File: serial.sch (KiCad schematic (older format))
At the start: 1 part

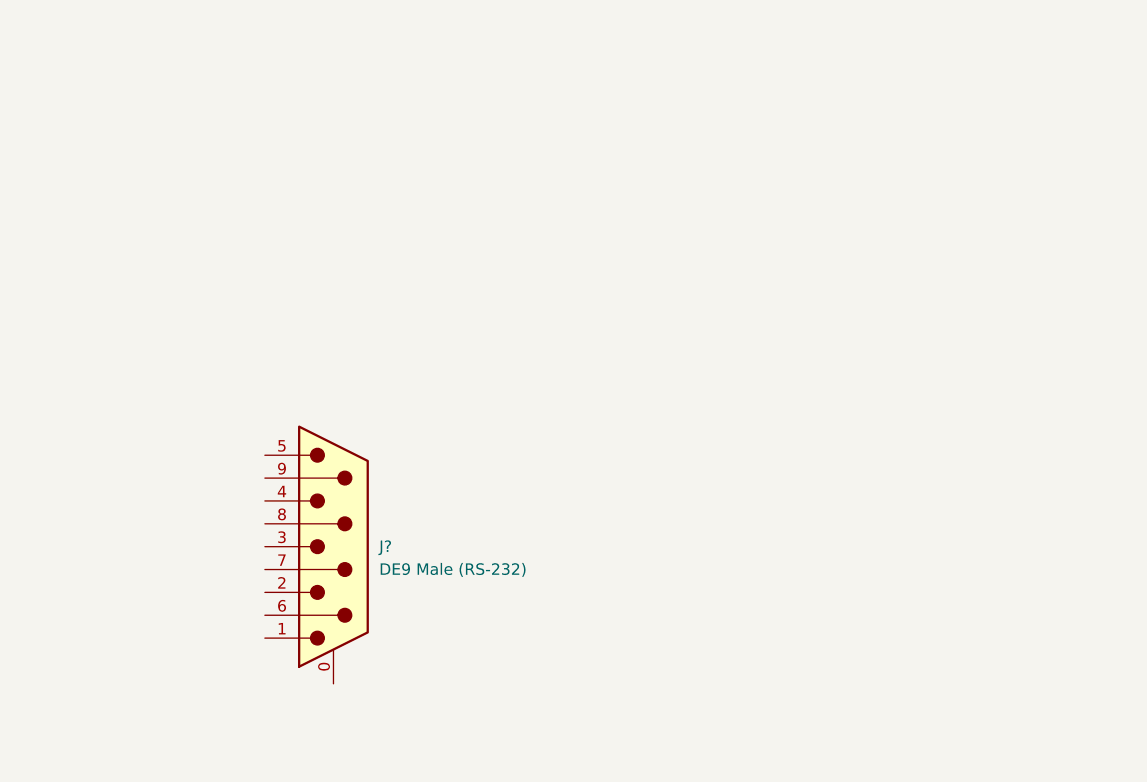
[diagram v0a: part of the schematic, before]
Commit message: Added some footprints. Basic board outline.
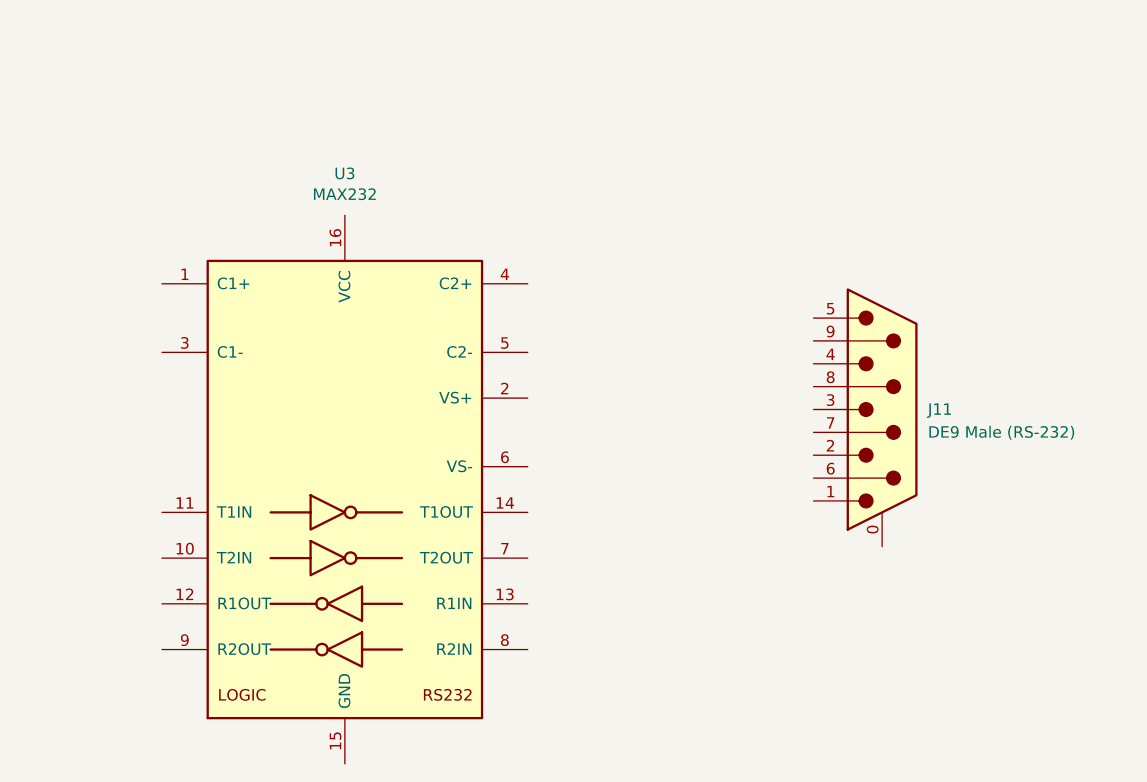
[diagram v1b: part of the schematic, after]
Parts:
- added U3: MAX232, Package_DIP:DIP-16_W7.62mm, symbol Interface_UART:MAX232
- gave numbers to parts that had none: 1
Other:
- moved on the sheet: J11
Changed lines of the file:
@@
 $Descr A4 11693 8268
 encoding utf-8
-Sheet 8 11
+Sheet 7 11
 Title "Neotron 32K"
 Date "2019-12-08"
@@
 L Connector:DB9_Male_MountingHoles J?
 U 1 1 5DF3B98B
-P 5550 3900
+P 7950 3300
 AR Path="/5DF3B98B" Ref="J?"  Part="1"
-AR Path="/5DF2601D/5DF3B98B" Ref="J?"  Part="1"
-F 0 "J?" H 5750 3900 50  0000 L CNN
-F 1 "DE9 Male (RS-232)" H 5750 3800 50  0000 L CNN
-F 2 "Connector_Dsub:DSUB-9_Male_Horizontal_P2.77x2.84mm_EdgePinOffset4.94mm_Housed_MountingHolesOffset7.48mm" H 5550 3900 50  0001 C CNN
-F 3 " ~" H 5550 3900 50  0001 C CNN
-	1    5550 3900
+AR Path="/5DF2601D/5DF3B98B" Ref="J11"  Part="1"
+F 0 "J11" H 8150 3300 50  0000 L CNN
+F 1 "DE9 Male (RS-232)" H 8150 3200 50  0000 L CNN
+F 2 "Connector_Dsub:DSUB-9_Male_Horizontal_P2.77x2.84mm_EdgePinOffset4.94mm_Housed_MountingHolesOffset7.48mm" H 7950 3300 50  0001 C CNN
+F 3 " ~" H 7950 3300 50  0001 C CNN
+	1    7950 3300
 	1    0    0    -1
 $EndComp
@@
 Text HLabel 1900 1550 0    50   Output ~ 0
 RS232_RTS_TO_MCU
+$Comp
+L Interface_UART:MAX232 U3
+U 1 1 5E0F5F91
+P 5600 3650
+F 0 "U3" H 5600 5031 50  0000 C CNN
+F 1 "MAX232" H 5600 4940 50  0000 C CNN
+F 2 "Package_DIP:DIP-16_W7.62mm" H 5650 2600 50  0001 L CNN
+F 3 "http://www.ti.com/lit/ds/symlink/max232.pdf" H 5600 3750 50  0001 C CNN
+	1    5600 3650
+	1    0    0    -1
+$EndComp
 $EndSCHEMATC

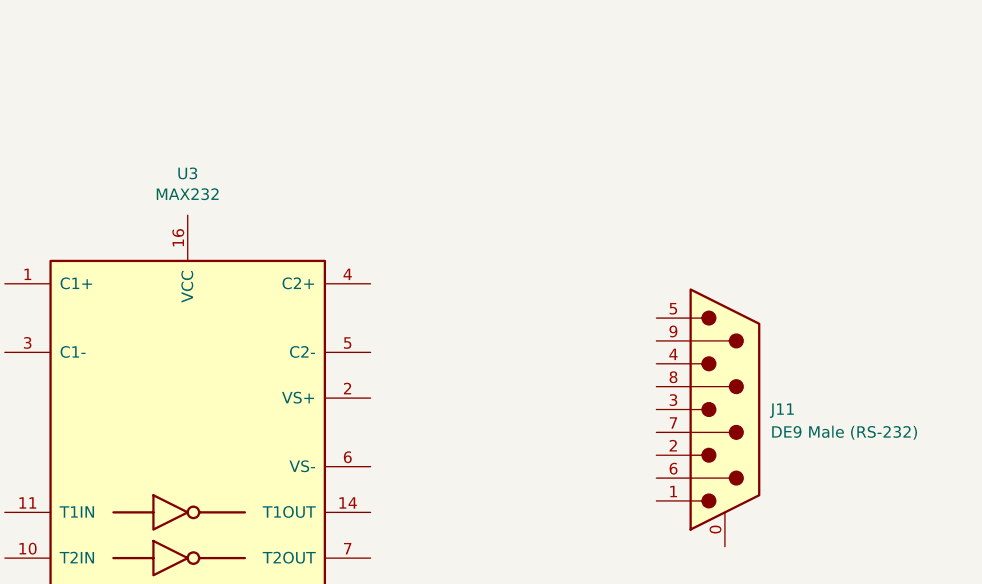
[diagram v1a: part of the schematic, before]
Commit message: Completed Power, SD, MIDI, Parallel and Joystick sheets.
Switch to sheet based 100x part numbering.
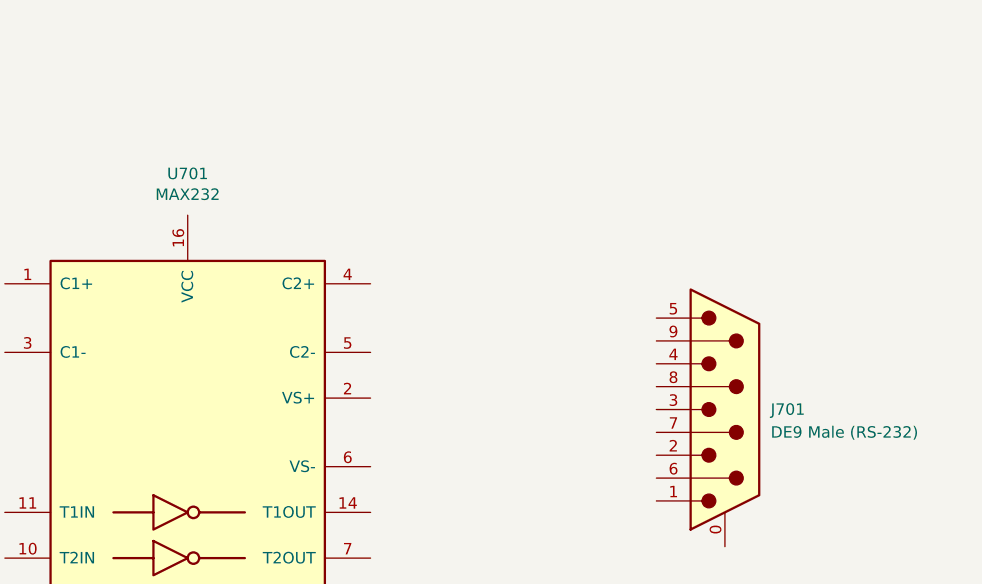
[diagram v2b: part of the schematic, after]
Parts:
- renumbered J11 to J701, U3 to U701
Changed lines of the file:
@@
 P 7950 3300
 AR Path="/5DF3B98B" Ref="J?"  Part="1"
-AR Path="/5DF2601D/5DF3B98B" Ref="J11"  Part="1"
-F 0 "J11" H 8150 3300 50  0000 L CNN
+AR Path="/5DF2601D/5DF3B98B" Ref="J701"  Part="1"
+F 0 "J701" H 8150 3300 50  0000 L CNN
 F 1 "DE9 Male (RS-232)" H 8150 3200 50  0000 L CNN
 F 2 "Connector_Dsub:DSUB-9_Male_Horizontal_P2.77x2.84mm_EdgePinOffset4.94mm_Housed_MountingHolesOffset7.48mm" H 7950 3300 50  0001 C CNN
@@
 RS232_RTS_TO_MCU
 $Comp
-L Interface_UART:MAX232 U3
+L Interface_UART:MAX232 U701
 U 1 1 5E0F5F91
 P 5600 3650
-F 0 "U3" H 5600 5031 50  0000 C CNN
+F 0 "U701" H 5600 5031 50  0000 C CNN
 F 1 "MAX232" H 5600 4940 50  0000 C CNN
 F 2 "Package_DIP:DIP-16_W7.62mm" H 5650 2600 50  0001 L CNN

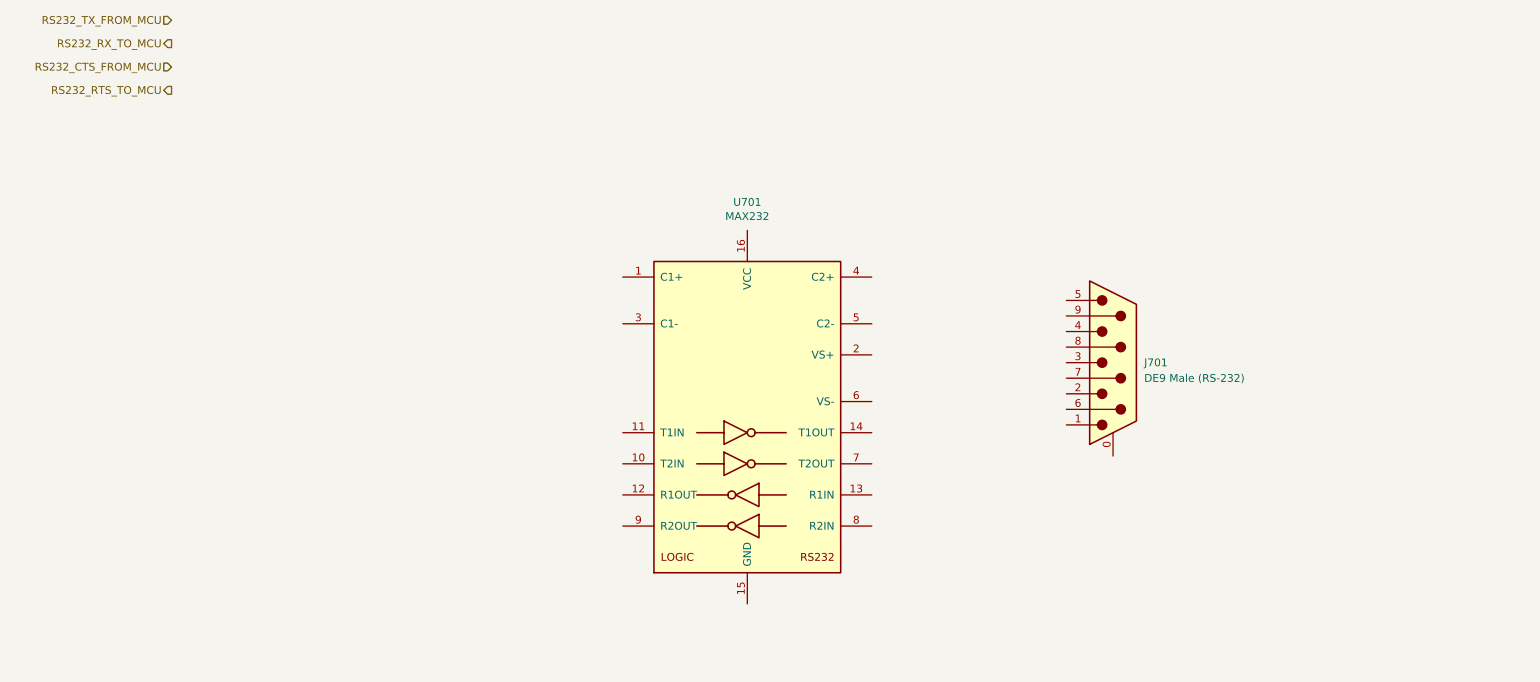
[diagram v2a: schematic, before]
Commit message: Schematic capture draft complete.
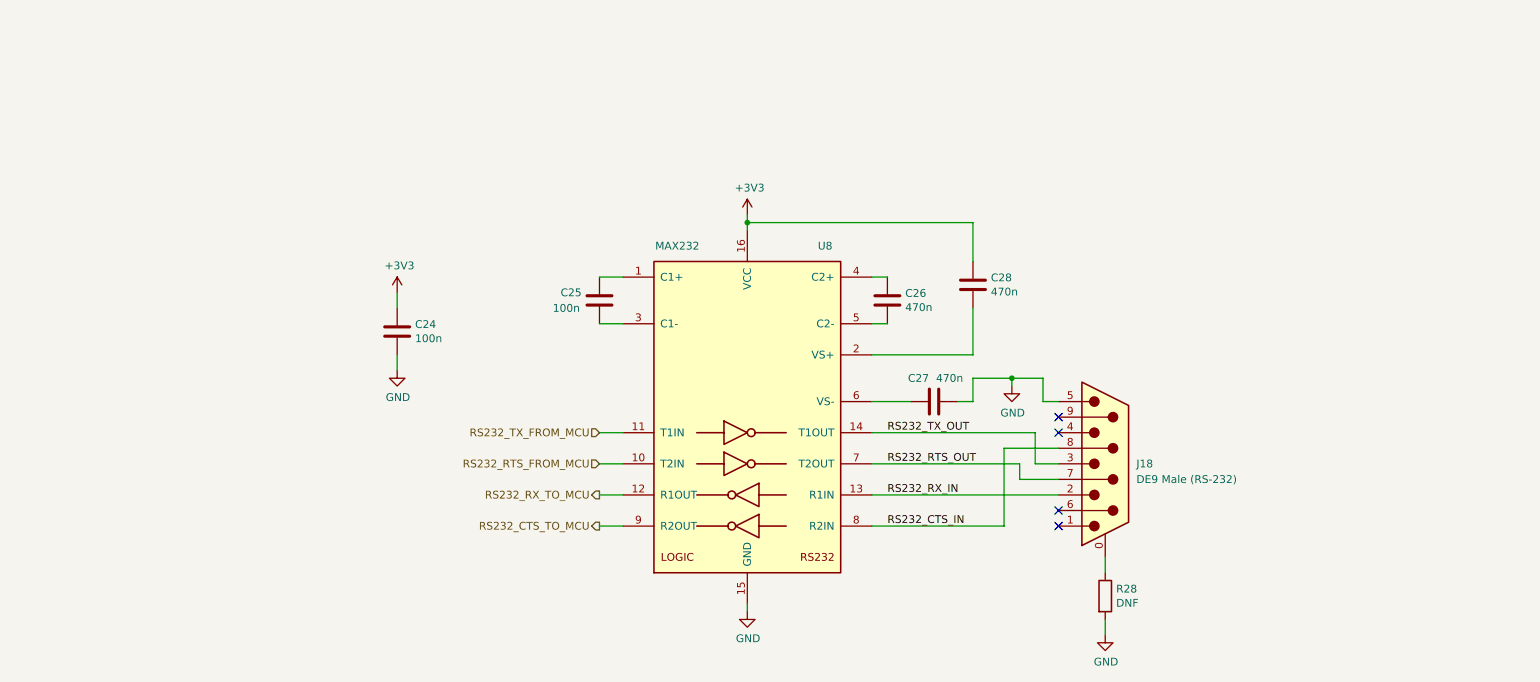
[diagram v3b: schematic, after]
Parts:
- added C24, C25: 100n, Capacitor_THT:C_Disc_D3.0mm_W2.0mm_P2.50mm, symbol Device:C
- added C26, C27, C28: 470n, Capacitor_THT:C_Disc_D3.0mm_W2.0mm_P2.50mm, symbol Device:C
- added R28: DNF, Resistor_THT:R_Axial_DIN0411_L9.9mm_D3.6mm_P12.70mm_Horizontal, symbol Device:R
- renumbered J701 to J18, U701 to U8
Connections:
- net RS232_RX_TO_MCU: now also U8.12 (R1OUT)
- net RS232_TX_FROM_MCU: now also U8.11 (T1IN)
- net at J18.0 (PAD): now also R28.1
- net RS232_RX_IN: now reaches J18.2
- net RS232_RX_IN: now also U8.13 (R1IN)
- net RS232_TX_OUT: now reaches J18.3
- net RS232_TX_OUT: now also U8.14 (T1OUT)
- net GND: now reaches J18.5
- net GND: now also U8.15 (GND), C24.1, C27.1, R28.2
- net RS232_RTS_OUT: now reaches J18.7
- net RS232_RTS_OUT: now also U8.7 (T2OUT)
- net RS232_CTS_IN: now reaches J18.8
- net RS232_CTS_IN: now also U8.8 (R2IN)
- net at U8.1 (C1+): now also C25.2
- net RS232_RTS_FROM_MCU: now reaches U8.10 (T2IN)
- net +3V3: now reaches U8.16 (VCC)
- net +3V3: now also C24.2, C28.1
- net at U8.2 (VS+): now also C28.2
- net at U8.3 (C1-): now also C25.1
- net at U8.4 (C2+): now also C26.1
- net at U8.5 (C2-): now also C26.2
- net at U8.6 (VS-): now also C27.2
- net RS232_CTS_TO_MCU: now reaches U8.9 (R2OUT)
- no-connect marks 0 -> 4
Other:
- moved on the sheet: J18

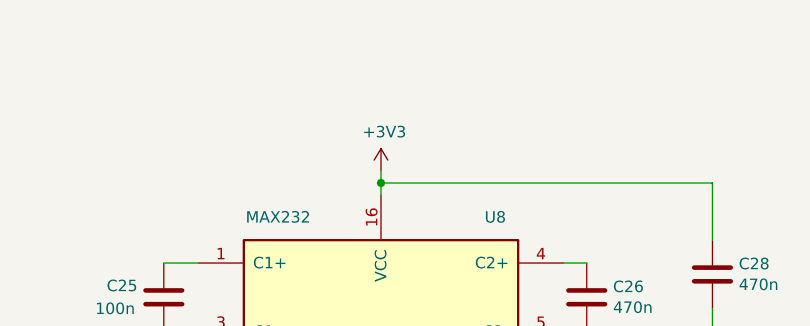
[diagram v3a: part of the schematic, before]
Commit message: Tidied up Atmega power. Added page titles.
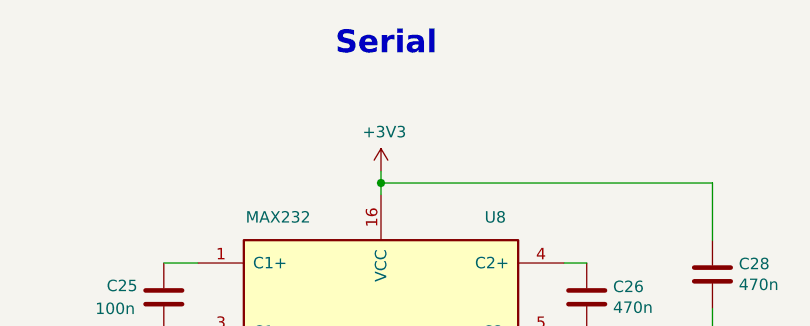
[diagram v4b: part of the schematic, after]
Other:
- note added: "Serial"
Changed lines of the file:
@@
 Sheet 10 10
 Title "Neotron 32K Main PCB"
-Date "2019-12-15"
-Rev "0.5"
+Date "2019-12-16"
+Rev "0.6"
 Comp "github.com/neotron-compute/Neotron-32-Hardware"
 Comment1 "Copyright (c) Jonathan 'theJPster' Pallant"
@@
 Wire Wire Line
 	3350 3250 3350 3350
+Text Notes 5400 1850 0    100  ~ 20
+Serial
 $EndSCHEMATC

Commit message: Work in progress.
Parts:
- removed J18: DE9 Male (RS-232), Connector_Dsub:DSUB-9_Male_Horizontal_P2.77x2.84mm_EdgePinOffset4.94mm_Housed_MountingHolesOffset7.48mm, symbol Connector:DB9_Male_MountingHoles
- removed R28: DNF, Resistor_THT:R_Axial_DIN0411_L9.9mm_D3.6mm_P12.70mm_Horizontal, symbol Device:R
- added J18: Conn_02x05_RS232, Connector_PinHeader_2.54mm:PinHeader_2x05_P2.54mm_Vertical, symbol Connector_Generic:Conn_02x05_Top_Bottom
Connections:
- net GND: now also J18.5 (Pin_5)
- net RS232_CTS_IN: now also J18.8 (Pin_8)
- net RS232_RTS_OUT: now also J18.7 (Pin_7)
- net RS232_RX_IN: now also J18.2 (Pin_2)
- net RS232_TX_OUT: now also J18.3 (Pin_3)
- no-connect marks 4 -> 5
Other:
- note added: "Header for IDC to DE9 Ribbon. Wired DTE."
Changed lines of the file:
@@
 Comment4 ""
 $EndDescr
-$Comp
-L Connector:DB9_Male_MountingHoles J?
-U 1 1 5DF3B98B
-P 7900 3950
-AR Path="/5DF3B98B" Ref="J?"  Part="1"
-AR Path="/5DF2601D/5DF3B98B" Ref="J18"  Part="1"
-F 0 "J18" H 8100 3950 50  0000 L CNN
-F 1 "DE9 Male (RS-232)" H 8100 3850 50  0000 L CNN
-F 2 "Connector_Dsub:DSUB-9_Male_Horizontal_P2.77x2.84mm_EdgePinOffset4.94mm_Housed_MountingHolesOffset7.48mm" H 7900 3950 50  0001 C CNN
-F 3 " ~" H 7900 3950 50  0001 C CNN
-	1    7900 3950
-	1    0    0    -1
-$EndComp
 Text HLabel 4650 3750 0    50   Input ~ 0
 RS232_TX_FROM_MCU
@@
 Wire Wire Line
 	4650 4350 4800 4350
-NoConn ~ 7600 3650
-NoConn ~ 7600 3750
-NoConn ~ 7600 4250
-NoConn ~ 7600 4350
-Wire Wire Line
-	7600 3950 7450 3950
-Wire Wire Line
-	7450 3750 6400 3750
-Wire Wire Line
-	7450 3750 7450 3950
-Wire Wire Line
-	7600 4150 6400 4150
 Text Label 6500 4350 0    50   ~ 0
 RS232_CTS_IN
@@
 Text Label 6500 3950 0    50   ~ 0
 RS232_RTS_OUT
-Wire Wire Line
-	6400 3950 7350 3950
-Wire Wire Line
-	7350 4050 7350 3950
-Wire Wire Line
-	7350 4050 7600 4050
-Wire Wire Line
-	6400 4350 7250 4350
-Wire Wire Line
-	7250 3850 7600 3850
-Wire Wire Line
-	7250 3850 7250 4350
 $Comp
 L power:GND #PWR072
@@
 Wire Wire Line
 	7300 3450 7300 3400
-Wire Wire Line
-	7300 3400 7500 3400
-Wire Wire Line
-	7500 3400 7500 3550
-Wire Wire Line
-	7500 3550 7600 3550
-$Comp
-L Device:R R28
-U 1 1 5E180C9A
-P 7900 4800
-F 0 "R28" H 7970 4846 50  0000 L CNN
-F 1 "DNF" H 7970 4755 50  0000 L CNN
-F 2 "Resistor_THT:R_Axial_DIN0411_L9.9mm_D3.6mm_P12.70mm_Horizontal" V 7830 4800 50  0001 C CNN
-F 3 "~" H 7900 4800 50  0001 C CNN
-	1    7900 4800
-	1    0    0    -1
-$EndComp
-$Comp
-L power:GND #PWR073
-U 1 1 5E181402
-P 7900 5050
-F 0 "#PWR073" H 7900 4800 50  0001 C CNN
-F 1 "GND" H 7905 4877 50  0000 C CNN
-F 2 "" H 7900 5050 50  0001 C CNN
-F 3 "" H 7900 5050 50  0001 C CNN
-	1    7900 5050
-	1    0    0    -1
-$EndComp
-Wire Wire Line
-	7900 5050 7900 4950
-Wire Wire Line
-	7900 4650 7900 4550
 $Comp
 L Device:C C26
@@
 Wire Wire Line
 	7050 3400 7300 3400
-Connection ~ 7300 3400
 Wire Wire Line
 	5600 2400 7050 2400
@@
 Text Notes 5400 1850 0    100  ~ 20
 Serial
+NoConn ~ 8400 3850
+NoConn ~ 7900 4250
+NoConn ~ 8400 4250
+NoConn ~ 7900 3950
+NoConn ~ 8400 3950
+$Comp
+L Connector_Generic:Conn_02x05_Top_Bottom J18
+U 1 1 5E02DBC9
+P 8100 4050
+F 0 "J18" H 8150 3625 50  0000 C CNN
+F 1 "Conn_02x05_RS232" H 8150 3716 50  0000 C CNN
+F 2 "Connector_PinHeader_2.54mm:PinHeader_2x05_P2.54mm_Vertical" H 8100 4050 50  0001 C CNN
+F 3 "~" H 8100 4050 50  0001 C CNN
+	1    8100 4050
+	1    0    0    1
+$EndComp
+$Comp
+L power:GND #PWR0101
+U 1 1 5E03D39E
+P 7700 3850
+F 0 "#PWR0101" H 7700 3600 50  0001 C CNN
+F 1 "GND" H 7700 3700 50  0000 C CNN
+F 2 "" H 7700 3850 50  0001 C CNN
+F 3 "" H 7700 3850 50  0001 C CNN
+	1    7700 3850
+	1    0    0    -1
+$EndComp
+Wire Wire Line
+	7700 3850 7700 3800
+Wire Wire Line
+	7700 3800 7850 3800
+Wire Wire Line
+	7850 3800 7850 3850
+Wire Wire Line
+	7850 3850 7900 3850
+Wire Wire Line
+	7500 3750 6400 3750
+Wire Wire Line
+	6400 4150 7900 4150
+Wire Wire Line
+	7900 4050 7500 4050
+Wire Wire Line
+	7500 3750 7500 4050
+Wire Wire Line
+	6400 3950 7350 3950
+Wire Wire Line
+	8700 4050 8400 4050
+Wire Wire Line
+	8600 4150 8400 4150
+Wire Wire Line
+	7250 4350 7250 4500
+Wire Wire Line
+	6400 4350 7250 4350
+Wire Wire Line
+	8600 4150 8600 4400
+Wire Wire Line
+	7350 3950 7350 4400
+Wire Wire Line
+	7350 4400 8600 4400
+Wire Wire Line
+	7250 4500 8700 4500
+Wire Wire Line
+	8700 4050 8700 4500
+Text Notes 8650 3900 0    50   ~ 0
+Header for IDC to DE9 Ribbon. Wired DTE.
 $EndSCHEMATC
